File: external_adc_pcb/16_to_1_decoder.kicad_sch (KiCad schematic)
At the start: 6 parts, among them U14 SN74AHC138RGYR, U15 SN74AHC138RGYR, U16 SN74LVC1G14DCKR_C19829630

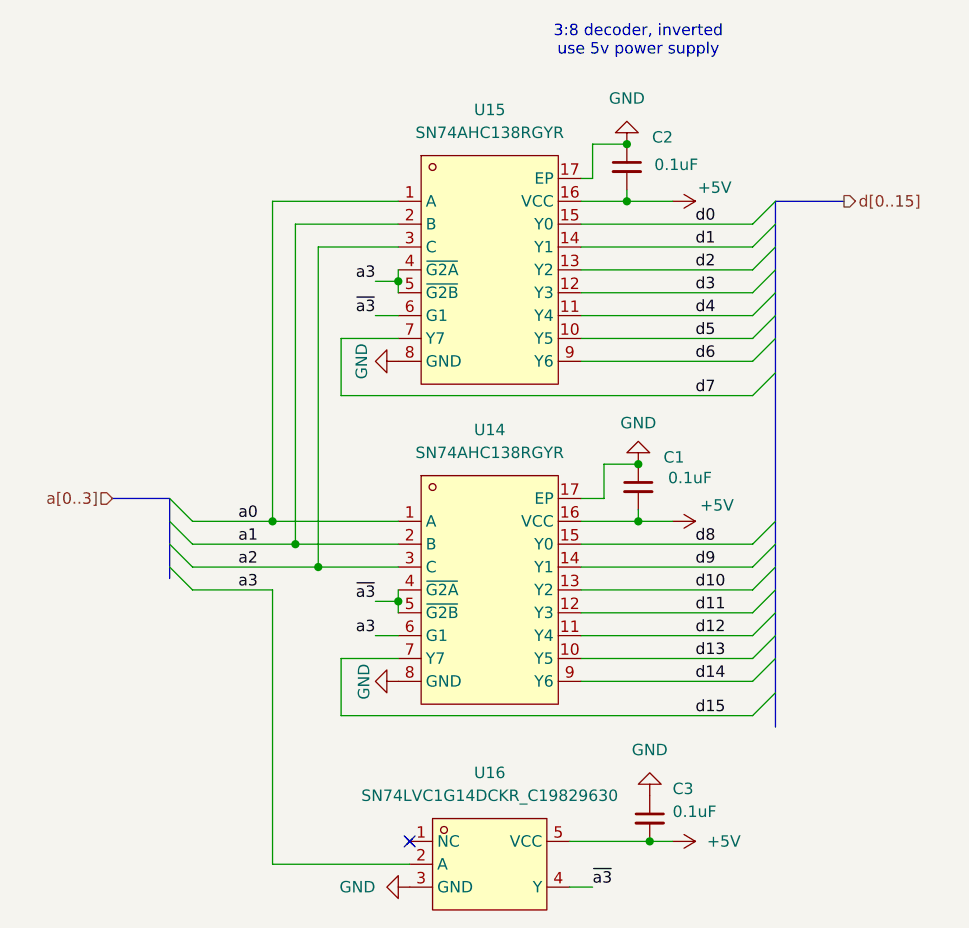
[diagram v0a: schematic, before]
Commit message: capitalize netnames; change and embed font
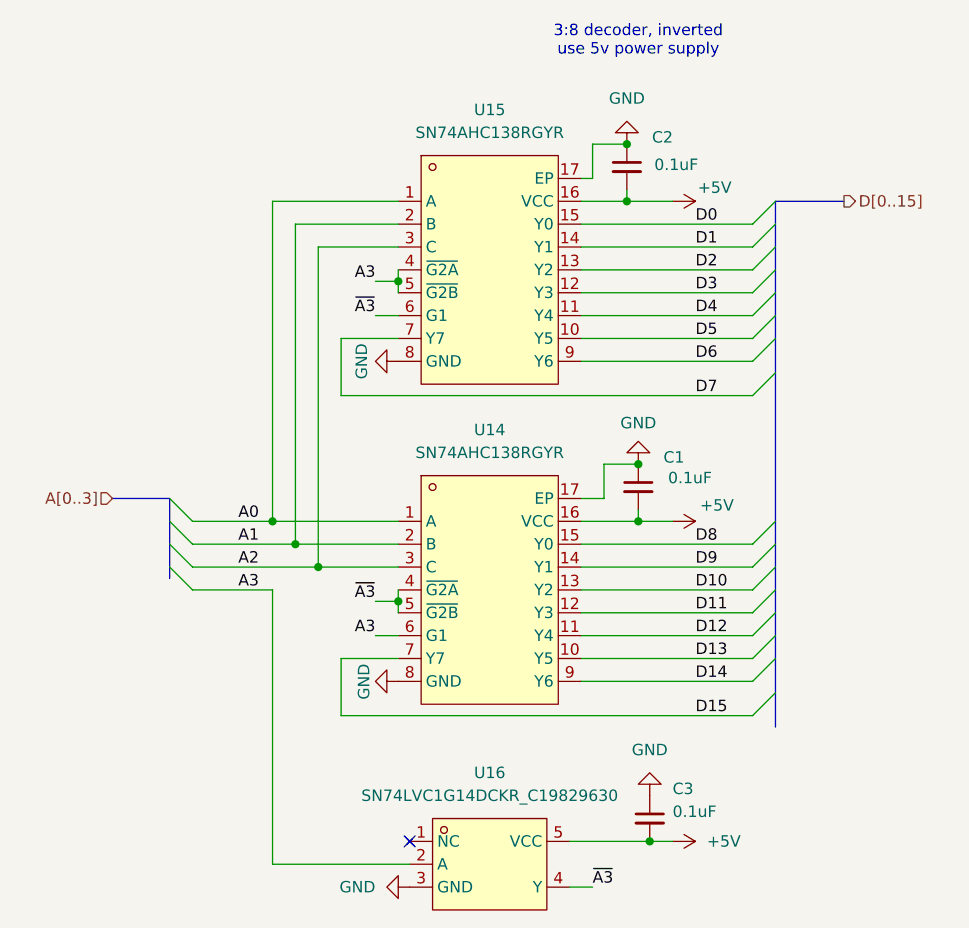
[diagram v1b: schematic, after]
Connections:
- net a0 renamed A0
- net a1 renamed A1
- net a2 renamed A2
- net a3 renamed A3
- net d0 renamed D0
- net d1 renamed D1
- net d10 renamed D10
- net d11 renamed D11
- net d12 renamed D12
- net d13 renamed D13
- net d14 renamed D14
- net d15 renamed D15
- net d2 renamed D2
- net d3 renamed D3
- net d4 renamed D4
- net d5 renamed D5
- net d6 renamed D6
- net d7 renamed D7
- net d8 renamed D8
- net d9 renamed D9
- net ~{a3} renamed ~{A3}
